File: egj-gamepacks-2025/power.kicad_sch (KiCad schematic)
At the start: 14 parts, among them J1 USB_B_Micro, U13 LD1117S18TR_SOT223, U3 NCP1117-3.3_SOT223, U5 USBLC6-2P6

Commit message: UPDATE: sync local schematic and board work
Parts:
- removed C23: 100u, Capacitor_SMD:C_0805_2012Metric, symbol Device:C
- removed D1: BAT54CW, Package_TO_SOT_SMD:SOT-323_SC-70, symbol Diode:BAT54CW
- removed TP7: TestPoint, TestPoint:TestPoint_Keystone_5015_Micro_Mini, symbol Connector:TestPoint
- removed U5: USBLC6-2P6, Package_TO_SOT_SMD:SOT-666, symbol Power_Protection:USBLC6-2P6
- U13: value LD1117S18TR_SOT223 -> AP7361C-28E; symbol Regulator_Linear:LD1117S18TR_SOT223 -> Regulator_Linear:AP7361C-28E
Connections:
- net +3V3_USB is gone; now on net +3V3: C6.1, U3.2 (VO)
- net +3V3: now also U13.1 (VI); no longer U13.3 (VI)
- net GND: now also U13.2 (GND); no longer U13.1 (GND)
- net +1V8 renamed +2V8
- net +2V8: now also U13.3 (VO); no longer U13.2 (VO)
- no-connect marks 2 -> 1

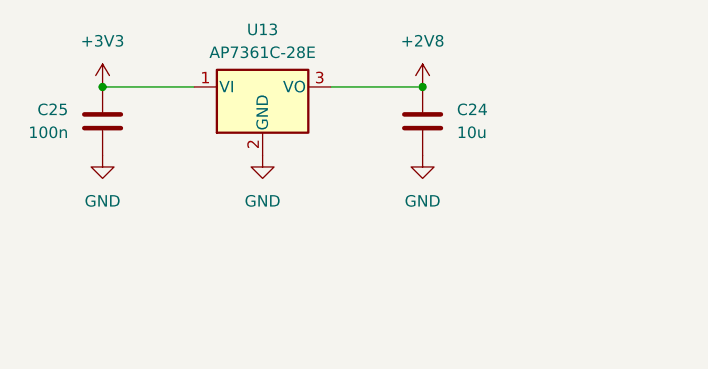
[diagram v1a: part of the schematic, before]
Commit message: FIX: schematic fixes, JLCPCB parts with LCSC numbers and GBA bus GPIO remap
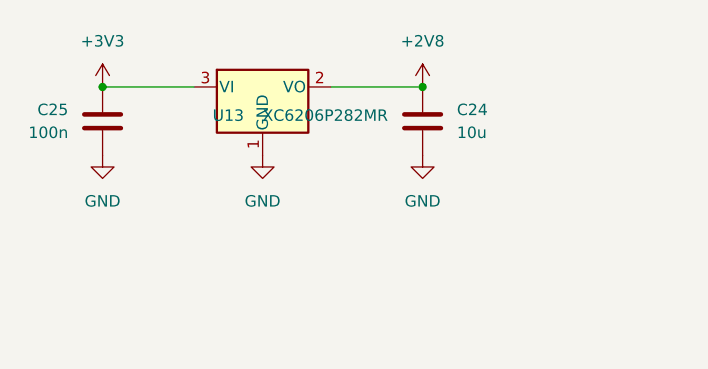
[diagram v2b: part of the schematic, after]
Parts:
- removed U13: AP7361C-28E, Package_TO_SOT_SMD:SOT-223-3_TabPin2, symbol Regulator_Linear:AP7361C-28E
- added U13: XC6206P282MR, Package_TO_SOT_SMD:SOT-23-3, symbol Regulator_Linear:XC6206PxxxMR
- C1, C24, C6: LCSC (none) -> C15850
- C25: LCSC (none) -> C49678
- J1: LCSC (none) -> C428495
- TP1, TP2, TP8: LCSC (none) -> C2906768
- U3: LCSC (none) -> C26537
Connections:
- net +2V8: now also U13.2 (VO)
- net +3V3: now also U13.3 (VI)
- net GND: now also U13.1 (GND)
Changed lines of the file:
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@@
+			)
+		)
+		(property "LCSC" "C15850"
+			(at 72.39 35.56 0)
+			(effects
+				(font
+					(size 1.27 1.27)
+				)
+				(hide yes)
 			)
 		)
@@
 			)
 		)
+		(property "LCSC" "C26537"
+			(at 99.06 81.28 0)
+			(effects
+				(font
+					(size 1.27 1.27)
+				)
+				(hide yes)
+			)
+		)
 		(property "Footprint" "Package_TO_SOT_SMD:SOT-223-3_TabPin2"
 			(at 99.06 76.2 0)
@@
 			)
 		)
+		(property "LCSC" "C428495"
+			(at 48.26 86.36 0)
+			(effects
+				(font
+					(size 1.27 1.27)
+				)
+				(hide yes)
+			)
+		)
 		(property "Footprint" "Connector_USB:USB_Micro-B_Amphenol_10103594-0001LF_Horizontal"
 			(at 52.07 87.63 0)
@@
 				)
 				(justify left)
+			)
+		)
+		(property "LCSC" "C2906768"
+			(at 191.77 50.8 0)
+			(effects
+				(font
+					(size 1.27 1.27)
+				)
+				(hide yes)
 			)
 		)
@@
 			)
 		)
+		(property "LCSC" "C49678"
+			(at 36.83 35.56 0)
+			(effects
+				(font
+					(size 1.27 1.27)
+				)
+				(hide yes)
+			)
+		)
 		(property "Footprint" "Capacitor_SMD:C_0805_2012Metric"
 			(at 37.7952 39.37 0)
@@
 				)
 				(justify left)
+			)
+		)
+		(property "LCSC" "C15850"
+			(at 81.28 86.36 0)
+			(effects
+				(font
+					(size 1.27 1.27)
+				)
+				(hide yes)
 			)
 		)
@@
 			)
 		)
+		(property "LCSC" "C2906768"
+			(at 191.77 77.47 0)
+			(effects
+				(font
+					(size 1.27 1.27)
+				)
+				(hide yes)
+			)
+		)
 		(property "Footprint" "TestPoint:TestPoint_Keystone_5015_Micro_Mini"
 			(at 196.85 77.47 0)
@@
 			)
 		)
+		(property "LCSC" "C2906768"
+			(at 191.77 60.96 0)
+			(effects
+				(font
+					(size 1.27 1.27)
+				)
+				(hide yes)
+			)
+		)
 		(property "Footprint" "TestPoint:TestPoint_Keystone_5015_Micro_Mini"
 			(at 196.85 60.96 0)
@@
 				)
 				(justify left)
+				(hide yes)
+			)
+		)
+		(property "LCSC" "C15850"
+			(at 116.84 86.36 0)
+			(effects
+				(font
+					(size 1.27 1.27)
+				)
 				(hide yes)
 			)
@@
 	)
 	(symbol
-		(lib_id "Regulator_Linear:AP7361C-28E")
-		(at 54.61 31.75 0)
-		(unit 1)
-		(exclude_from_sim no)
-		(in_bom yes)
-		(on_board yes)
-		(dnp no)
-		(fields_autoplaced yes)
-		(property "Reference" "U13"
-			(at 54.61 25.4 0)
-			(effects
-				(font
-					(size 1.27 1.27)
-				)
-			)
-		)
-		(property "Value" "AP7361C-28E"
-			(at 54.61 27.94 0)
-			(effects
-				(font
-					(size 1.27 1.27)
-				)
-			)
-		)
-		(property "Footprint" "Package_TO_SOT_SMD:SOT-223-3_TabPin2"
-			(at 54.61 26.67 0)
-			(effects
-				(font
-					(size 1.27 1.27)
-				)
-				(hide yes)
-			)
-		)
-		(property "Datasheet" "https://www.diodes.com/assets/Datasheets/AP7361C.pdf"
-			(at 57.15 38.1 0)
-			(effects
-				(font
-					(size 1.27 1.27)
-				)
-				(hide yes)
-			)
-		)
-		(property "Description" "1A Low Dropout regulator, positive, 2.8V fixed output, SOT-223"
-			(at 54.61 31.75 0)
-			(effects
-				(font
-					(size 1.27 1.27)
-				)
-				(hide yes)
-			)
-		)
-		(pin "3"
-		)
-		(pin "1"
-		)
-		(pin "2"
-		)
-		(instances
-			(project "egj-gamepacks-2025"
-				(path "/2a9955bc-bd61-45c5-81ed-8dd8c377b4a4/f0d934e7-dbe2-4b9a-81ab-c80699e3b9a0"
-					(reference "U13")
-					(unit 1)
-				)
-			)
-		)
-	)
-	(symbol
 		(lib_name "+3V3_2")
 		(lib_id "power:+3V3")
@@
 		)
 	)
+  (symbol (lib_id "Regulator_Linear:XC6206PxxxMR") (at 54.61 31.75 0) (unit 1)
+    (exclude_from_sim no) (in_bom yes) (on_board yes) (dnp no)
+    (property "Reference" "U13"
+      (at 50.8 34.925 0)
+      (show_name no)
+      (do_not_autoplace no)
+      (effects
+    				(font
+    					(size 1.27 1.27)
+    				)
+    			)
+    )
+    (property "Value" "XC6206P282MR"
+      (at 54.61 34.925 0)
+      (show_name no)
+      (do_not_autoplace no)
+      (effects
+    				(font
+    					(size 1.27 1.27)
+    				)
+    				(justify left)
+    			)
+    )
+		(property "LCSC" "C347374"
+			(at 54.61 31.75 0)
+			(effects
+				(font
+					(size 1.27 1.27)
+				)
+				(hide yes)
+			)
+		)
+    (property "Footprint" "Package_TO_SOT_SMD:SOT-23-3"
+      (at 54.61 37.465 0)
+      (hide yes)
+      (show_name no)
+      (do_not_autoplace no)
+      (effects
+    				(font
+    					(size 1.27 1.27)
+    					(italic yes)
+    				)
+    			)
+    )
+    (property "Datasheet" "https://www.diodes.com/assets/Datasheets/AP7361C.pdf"
+      (at 54.61 31.75 0)
+      (hide yes)
+      (show_name no)
+      (do_not_autoplace no)
+      (effects
+    				(font
+    					(size 1.27 1.27)
+    				)
+    			)
+    )
+    (property "Description" "1A Low Dropout regulator, positive, 2.8V fixed output, SOT-223"
+      (at 54.61 31.75 0)
+      (hide yes)
+      (show_name no)
+      (do_not_autoplace no)
+      (effects
+    				(font
+    					(size 1.27 1.27)
+    				)
+    			)
+    )
+    (pin "1")
+    (pin "2")
+    (pin "3")
+    (instances
+      (project "egj-gamepacks-2025"
+        (path "/2a9955bc-bd61-45c5-81ed-8dd8c377b4a4/f0d934e7-dbe2-4b9a-81ab-c80699e3b9a0"
+          (reference "U13")
+          (unit 1)
+        )
+      )
+    )
+  )
 )

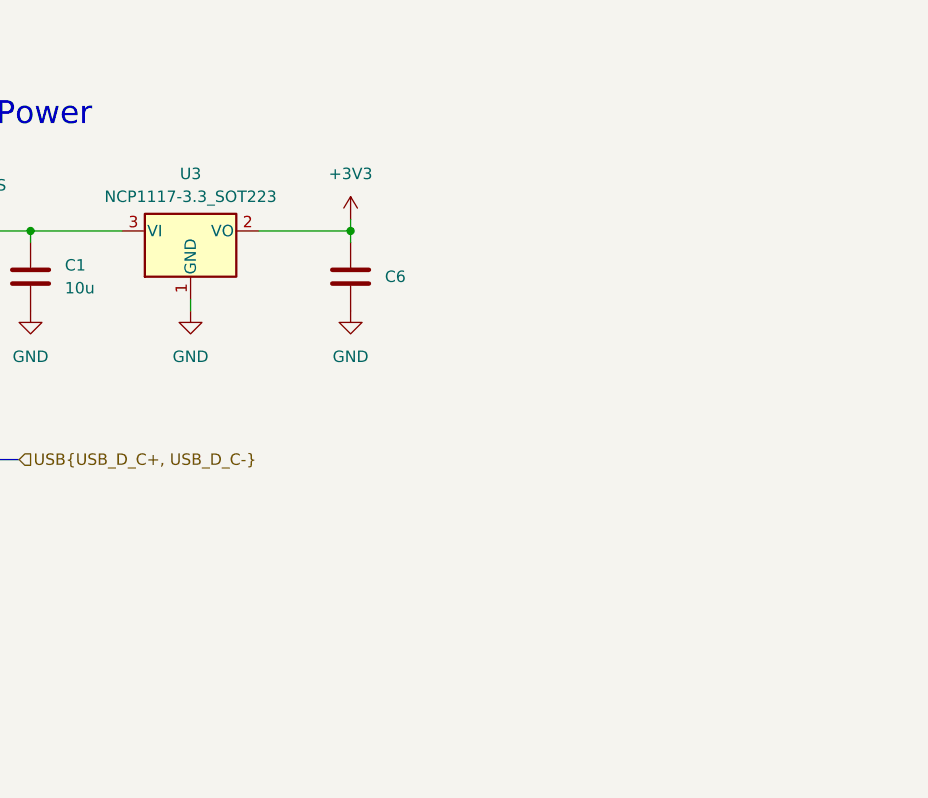
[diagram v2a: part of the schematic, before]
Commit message: ADD: TPS2116 power path so the cartridge runs from console, USB or both
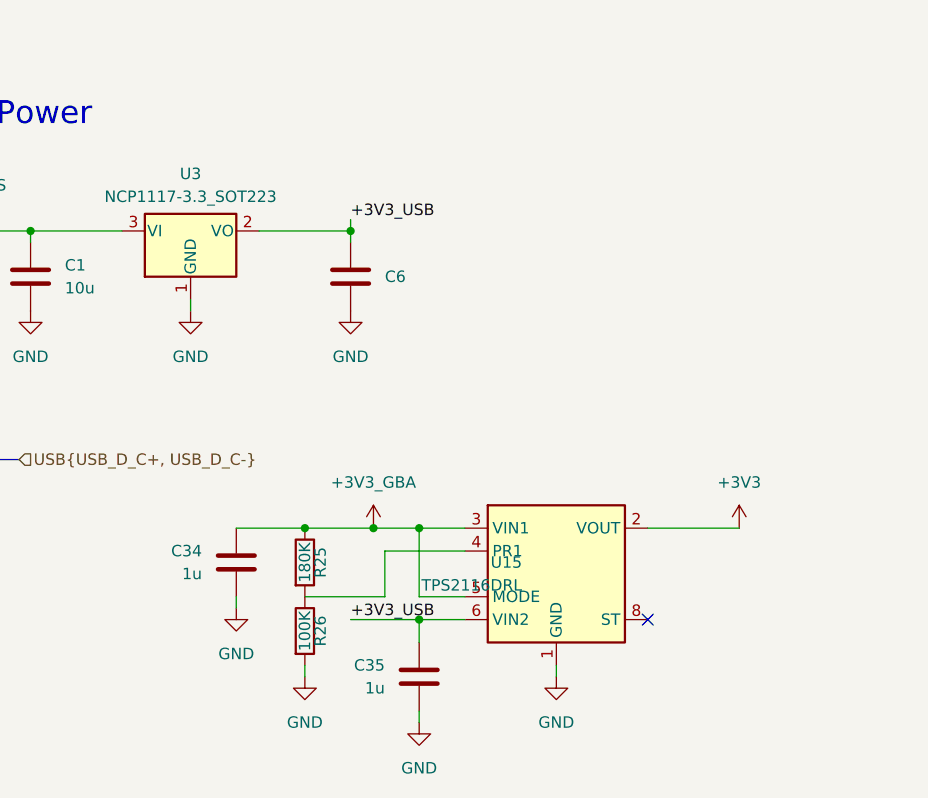
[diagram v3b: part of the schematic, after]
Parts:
- added C34, C35: 1u, Capacitor_SMD:C_0402_1005Metric, symbol Device:C
- added R25: 180K, Resistor_SMD:R_0402_1005Metric, symbol Device:R
- added R26: 100K, Resistor_SMD:R_0402_1005Metric, symbol Device:R
- added U15: TPS2116DRL, Package_TO_SOT_SMD:SOT-583-8, symbol Power_Management:TPS2116DRL
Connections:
- net +3V3: now also U15.2 (VOUT), U15.7 (VOUT); no longer C6.1, U3.2 (VO)
- net +3V3_GBA: now also C34.1, R25.1, U15.3 (VIN1), U15.5 (MODE)
- net GND: now also C34.2, C35.2, R26.2, U15.1 (GND)
- new net: R25.2, R26.1, U15.4 (PR1)
- new net +3V3_USB: C35.1, C6.1, U15.6 (VIN2), U3.2 (VO)
- no-connect marks 1 -> 2
